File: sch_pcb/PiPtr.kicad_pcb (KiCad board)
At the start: 4 copper layers, 101.6 x 141.7 mm, 383 parts, among them J101 GLOBAL_LINK_LEFT, J102 GLOBAL_LINK_RIGHT, J107 RASPBERRY_PI, J111 FP_PIXEL, J112 AM2302, J204 DE9F, J305 AUX_IO_1, J306 SPARE, J307 SPARE, J308 AUX_IO_2, J311 I2C1_5V, J312 RTC, J315 OLED_SSD1306, J404 DE9F, J501 MicroUSB, P301 Chassis, Q101 BSS138, Q102 BSS138, Q103 BSS138, Q104 BSS138, Q105 BSS138, Q201 BSS138, Q202 BSS138, Q203 BSS138, Q401 BSS138, Q402 BSS138, Q403 BSS138, Q501 BSR315PH6327XTSA1, U101 MCP23008, U102 IP4234CZ6, U103 MCP4351, U104 74HCT138, U105 74LV1T125, U106 MCP6004T, U107 MCP4351, U108 74LVC4066, U109 74LVC1G3157, U110 74LV1T125, U111 74LV1T125, U112 74LV1T125, U113 74LV1T125, U201 MCP6004T, U202 74LVC1G3157, U203 74LVC1G3157, U204 74LVC4066, U205 MCP6004T, U206 74LVC1G3157, U207 MCP6S26, U208 MCP23008, U301 MCP23017, U304 MCP3008, U305 MCP1703A-2502/MB, U306 TPS54302, U307 IP4234CZ6, U308 IP4234CZ6, U401 MCP6004T, U402 74LVC1G3157, U403 74LVC1G3157, U404 74LVC4066, U405 MCP6004T, U406 74LVC1G3157, U407 MCP6S26, U408 MCP23008, U501 CM108B, U502 CM108B, U503 TUSB2036, U504 MCP1703A-3302/MB, U505 CM108B, Y501 6MHz

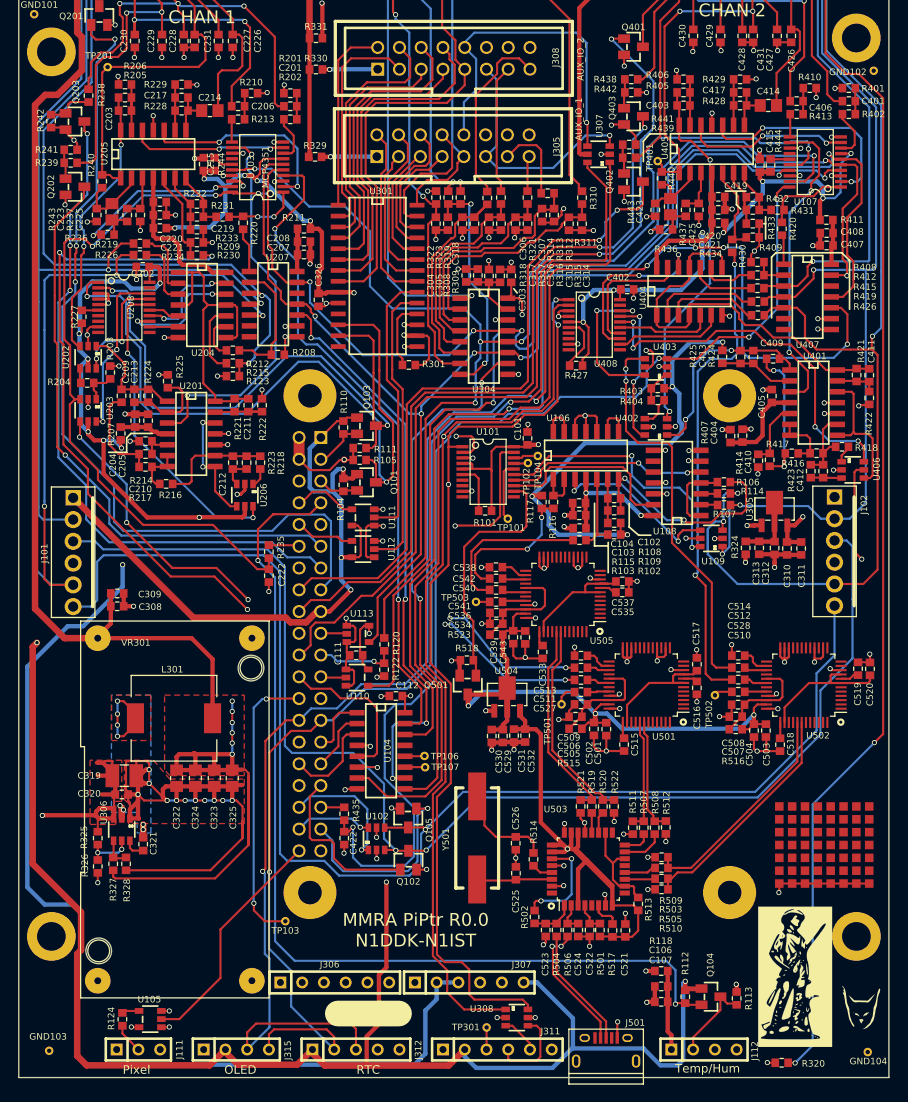
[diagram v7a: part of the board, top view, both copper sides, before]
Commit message: Add minimum load on 2v5 regulator.  Update gain to soundcard 1 and 2
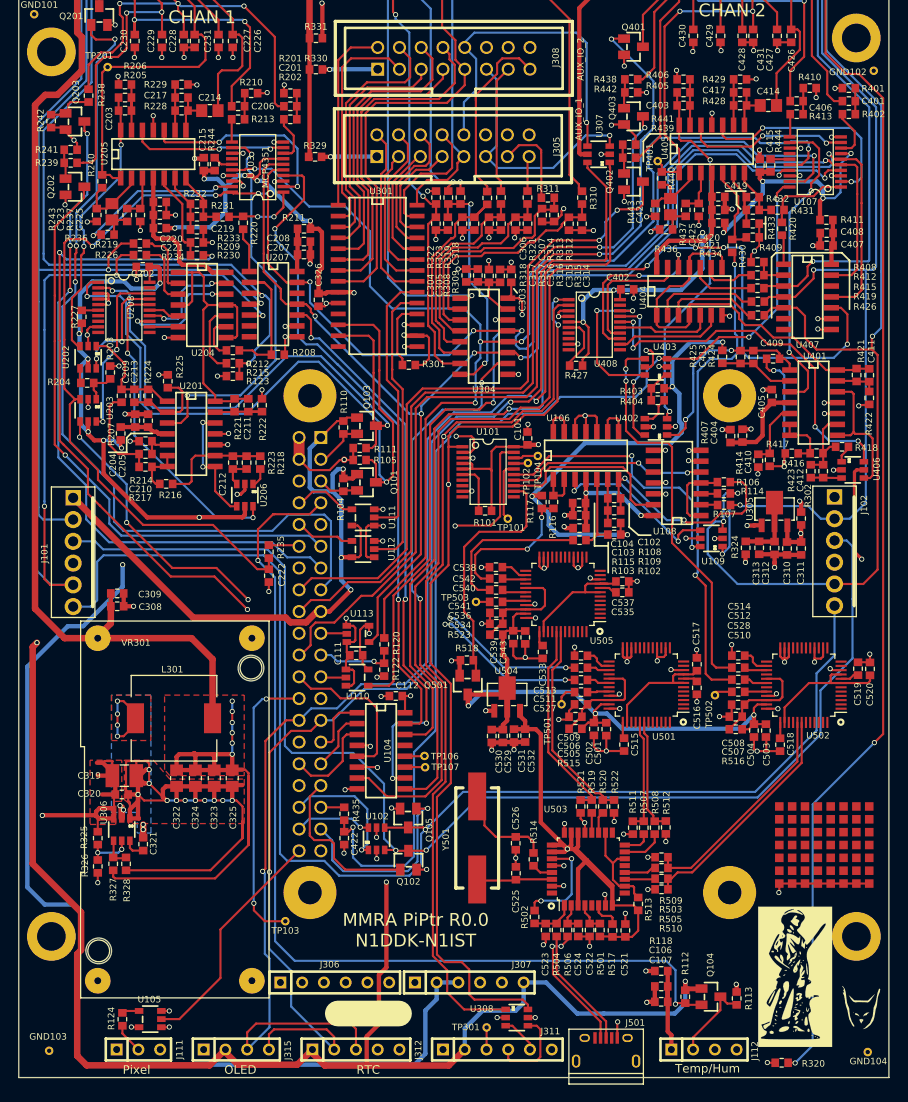
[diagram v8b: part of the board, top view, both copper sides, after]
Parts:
- added R302: 1k, lib:smd0603, F.Cu at (148.5, 104.4)
- R204, R404: value 20k -> 3k3
- moved R311 0.53 mm to (118.9, 66.9)
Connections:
- J112 pad 3: Net-(J112-Pad3) -> (no net)
- J305 pad 16: Net-(J305-Pad16) -> (no net)
- J307 pad 1: Net-(J307-Pad1) -> (no net)
- J308 pad 16: Net-(J308-Pad16) -> (no net)
- J312 pad 4: (no net) -> Net-(J312-Pad4)
- J501 pad 1: Net-(J501-Pad1) -> (no net)
- J501 pad 4: Net-(J501-Pad4) -> (no net)
- MTG301 pad 1: Net-(MTG301-Pad1) -> (no net)
- MTG302 pad 1: Net-(MTG302-Pad1) -> (no net)
- MTG303 pad 1: Net-(MTG303-Pad1) -> (no net)
- MTG304 pad 1: Net-(MTG304-Pad1) -> (no net)
- U101 pad 10: (no net) -> Net-(U101-Pad10)
- U101 pad 11: (no net) -> Net-(U101-Pad11)
- U101 pad 7: (no net) -> Net-(U101-Pad7)
- U101 pad 8: (no net) -> Net-(U101-Pad8)
- U104 pad 13: Net-(U104-Pad13) -> (no net)
- U108 pad 10: (no net) -> Net-(U108-Pad10)
- U108 pad 9: (no net) -> Net-(U108-Pad9)
- U207 pad 12: Net-(U207-Pad12) -> (no net)
- U207 pad 6: Net-(U207-Pad6) -> (no net)
- U207 pad 7: Net-(U207-Pad7) -> (no net)
- U208 pad 10: (no net) -> Net-(U208-Pad10)
- U208 pad 11: (no net) -> Net-(U208-Pad11)
- U208 pad 19: (no net) -> Net-(U208-Pad19)
- U208 pad 7: (no net) -> Net-(U208-Pad7)
- U208 pad 8: (no net) -> Net-(U208-Pad8)
- U407 pad 12: Net-(U407-Pad12) -> (no net)
- U407 pad 6: Net-(U407-Pad6) -> (no net)
- U407 pad 7: Net-(U407-Pad7) -> (no net)
- U408 pad 10: Net-(U408-Pad10) -> (no net)
- U408 pad 11: Net-(U408-Pad11) -> (no net)
- U408 pad 19: Net-(U408-Pad19) -> (no net)
- U408 pad 7: Net-(U408-Pad7) -> (no net)
- U408 pad 8: Net-(U408-Pad8) -> (no net)
- U501 pad 1: Net-(U501-Pad1) -> (no net)
- U501 pad 11: Net-(U501-Pad11) -> (no net)
- U501 pad 12: Net-(U501-Pad12) -> (no net)
- U501 pad 13: Net-(U501-Pad13) -> (no net)
- U501 pad 15: Net-(U501-Pad15) -> (no net)
- U501 pad 17: Net-(U501-Pad17) -> (no net)
- U501 pad 18: Net-(U501-Pad18) -> (no net)
- U501 pad 19: Net-(U501-Pad19) -> (no net)
- U501 pad 2: Net-(U501-Pad2) -> (no net)
- U501 pad 20: Net-(U501-Pad20) -> (no net)
- U501 pad 21: Net-(U501-Pad21) -> (no net)
- U501 pad 25: Net-(U501-Pad25) -> (no net)
- U501 pad 28: Net-(U501-Pad28) -> (no net)
- U501 pad 3: Net-(U501-Pad3) -> (no net)
- U501 pad 31: Net-(U501-Pad31) -> (no net)
- U501 pad 39: Net-(U501-Pad39) -> (no net)
- U501 pad 4: Net-(U501-Pad4) -> (no net)
- U501 pad 40: Net-(U501-Pad40) -> (no net)
- U501 pad 43: Net-(U501-Pad43) -> (no net)
- U501 pad 44: Net-(U501-Pad44) -> (no net)
- U501 pad 45: Net-(U501-Pad45) -> (no net)
- U501 pad 46: Net-(U501-Pad46) -> (no net)
- U501 pad 47: Net-(U501-Pad47) -> (no net)
- U501 pad 48: Net-(U501-Pad48) -> (no net)
- U501 pad 5: Net-(U501-Pad5) -> (no net)
- U501 pad 6: Net-(U501-Pad6) -> (no net)
- U502 pad 1: Net-(U502-Pad1) -> (no net)
- U502 pad 11: Net-(U502-Pad11) -> (no net)
- U502 pad 12: Net-(U502-Pad12) -> (no net)
- U502 pad 13: Net-(U502-Pad13) -> (no net)
- U502 pad 15: Net-(U502-Pad15) -> (no net)
- U502 pad 17: Net-(U502-Pad17) -> (no net)
- U502 pad 18: Net-(U502-Pad18) -> (no net)
- U502 pad 19: Net-(U502-Pad19) -> (no net)
- U502 pad 2: Net-(U502-Pad2) -> (no net)
- U502 pad 20: Net-(U502-Pad20) -> (no net)
- U502 pad 21: Net-(U502-Pad21) -> (no net)
- U502 pad 25: Net-(U502-Pad25) -> (no net)
- U502 pad 28: Net-(U502-Pad28) -> (no net)
- U502 pad 3: Net-(U502-Pad3) -> (no net)
- U502 pad 31: Net-(U502-Pad31) -> (no net)
- U502 pad 39: Net-(U502-Pad39) -> (no net)
- U502 pad 4: Net-(U502-Pad4) -> (no net)
- U502 pad 40: Net-(U502-Pad40) -> (no net)
- U502 pad 43: Net-(U502-Pad43) -> (no net)
- U502 pad 44: Net-(U502-Pad44) -> (no net)
- U502 pad 45: Net-(U502-Pad45) -> (no net)
- U502 pad 46: Net-(U502-Pad46) -> (no net)
- U502 pad 47: Net-(U502-Pad47) -> (no net)
- U502 pad 48: Net-(U502-Pad48) -> (no net)
- U502 pad 5: Net-(U502-Pad5) -> (no net)
- U502 pad 6: Net-(U502-Pad6) -> (no net)
- U503 pad 13: Net-(U503-Pad13) -> (no net)
- U503 pad 17: Net-(U503-Pad17) -> (no net)
- U503 pad 32: Net-(U503-Pad32) -> (no net)
- U503 pad 5: Net-(U503-Pad5) -> (no net)
- U503 pad 9: Net-(U503-Pad9) -> (no net)
- U505 pad 1: (no net) -> Net-(U505-Pad1)
- U505 pad 11: (no net) -> Net-(U505-Pad11)
- U505 pad 12: (no net) -> Net-(U505-Pad12)
- U505 pad 13: (no net) -> Net-(U505-Pad13)
- U505 pad 15: (no net) -> Net-(U505-Pad15)
- U505 pad 17: (no net) -> Net-(U505-Pad17)
- U505 pad 18: (no net) -> Net-(U505-Pad18)
- U505 pad 19: (no net) -> Net-(U505-Pad19)
- U505 pad 2: (no net) -> Net-(U505-Pad2)
- U505 pad 20: (no net) -> Net-(U505-Pad20)
- U505 pad 21: (no net) -> Net-(U505-Pad21)
- U505 pad 25: (no net) -> Net-(U505-Pad25)
- U505 pad 28: (no net) -> Net-(U505-Pad28)
- U505 pad 3: (no net) -> Net-(U505-Pad3)
- U505 pad 31: (no net) -> Net-(U505-Pad31)
- U505 pad 39: (no net) -> Net-(U505-Pad39)
- U505 pad 4: (no net) -> Net-(U505-Pad4)
- U505 pad 40: (no net) -> Net-(U505-Pad40)
- U505 pad 43: (no net) -> Net-(U505-Pad43)
- U505 pad 44: (no net) -> Net-(U505-Pad44)
- U505 pad 45: (no net) -> Net-(U505-Pad45)
- U505 pad 46: (no net) -> Net-(U505-Pad46)
- U505 pad 47: (no net) -> Net-(U505-Pad47)
- U505 pad 48: (no net) -> Net-(U505-Pad48)
- U505 pad 5: (no net) -> Net-(U505-Pad5)
- U505 pad 6: (no net) -> Net-(U505-Pad6)
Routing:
- net +3V3: track 541.3 -> 528.5 mm
- net /CH2/TONE_FROM_PI: track 129.7 -> 125.8 mm
- net Net-(R208-Pad2): track 14.9 -> 16.2 mm
- net GND: track 365.2 -> 366.4 mm, vias 153 -> 154
- net /Spares, GPIO, and ADC/ADC2: track 9.85 -> 10.4 mm
- net Net-(C315-Pad1): track 26.9 -> 26.4 mm
- net SCLK_5: track 180.4 -> 180.0 mm, vias 6 -> 5
